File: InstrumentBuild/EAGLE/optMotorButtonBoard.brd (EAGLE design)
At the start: 66 x 33.1 mm, 12 parts

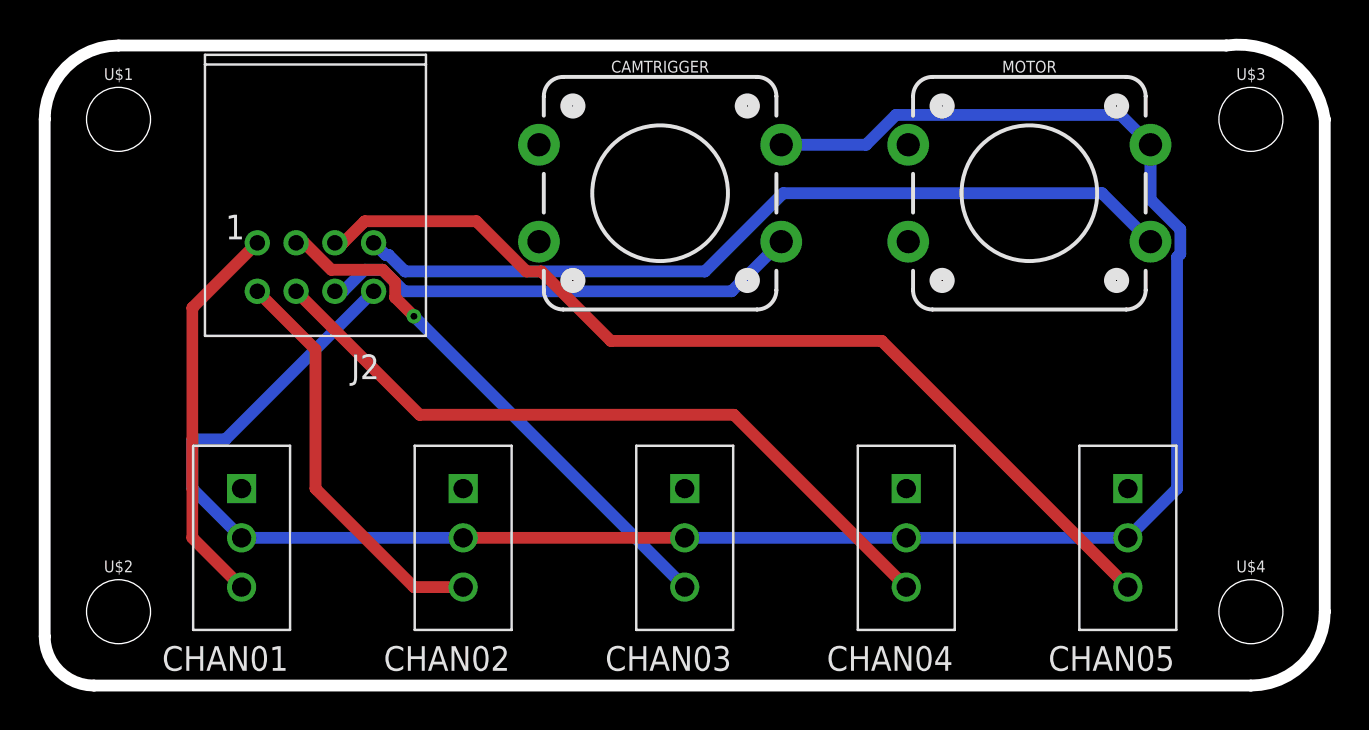
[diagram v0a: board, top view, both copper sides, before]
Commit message: Updated top silk and added board's name to top.
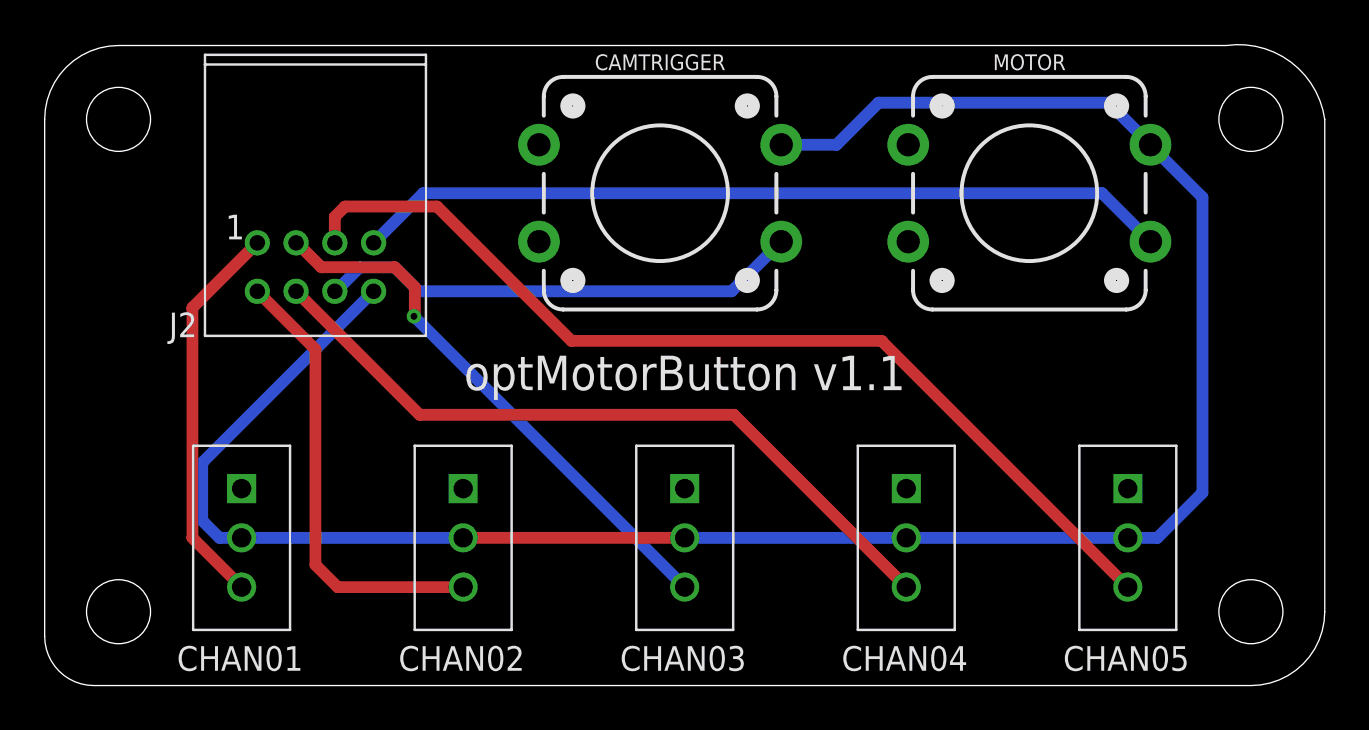
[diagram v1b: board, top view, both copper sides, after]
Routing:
- net C2: track 21.1 -> 23.5 mm
- net VCC: track 106.7 -> 108.3 mm
- net C5: track 49.2 -> 50.6 mm
- net BTN: track 43.4 -> 42.2 mm
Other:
- board text added: "optMotorButton v1.1"
